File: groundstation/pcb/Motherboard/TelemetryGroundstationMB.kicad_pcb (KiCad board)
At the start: 4 copper layers, 95 x 95 mm, 146 parts, among them J1 USB-C, J2 USB-C, J3 RFPC-SMA28-F, J4 RFPC-SMA28-F, M1 M4 Mounting Hole, M2 M4 Mounting Hole, M3 M4 Mounting Hole, M4 M4 Mounting Hole, Q1 NPN, U1 CP2102N, U2 CP2102N, U3 RC1780HP-RC232, U4 RC1701HP-RC232, U5 AVR128DB64x-xPT, U6 W25Q80DVSSIG

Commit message: add motherboard pcb
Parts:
- removed C15: 1 uf, Capacitor_SMD:C_0805_2012Metric_Pad1.18x1.45mm_HandSolder
- removed D17: yellow, LED_SMD:LED_0805_2012Metric_Pad1.15x1.40mm_HandSolder
- removed D18: D, Diode_SMD:D_SOD-123
- removed D19, D20, D21, D22, D23, D24: red, LED_SMD:LED_0805_2012Metric_Pad1.15x1.40mm_HandSolder
- removed D25, D26: orange, LED_SMD:LED_0805_2012Metric_Pad1.15x1.40mm_HandSolder
- removed JL1: Stackable Socket 1x8, Footprints:JL1
- removed JL2: Stackable Socket 1x8, Footprints:JL2
- removed JL3: Stackable Socket 1x8, Footprints:JL3
- removed JL4: Stackable Socket 1x8, Footprints:JL4
- removed JR1: Stackable Socket 1x8, Footprints:JR1
- removed JR2: Stackable Socket 1x8, Footprints:JR2
- removed JR3: Stackable Socket 1x8, Footprints:JR3
- removed JR4: Stackable Socket 1x8, Footprints:JR4
- removed LS1: Buzzer CMT-0525-75-SMT-TR, Footprints:Buzzer XDCR_CMT-0525-75-SMT-TR
- removed Q1: NPN, Package_TO_SOT_SMD:SOT-23
- removed R40, R41, R42, R49, R50: 5k6, Resistor_SMD:R_0805_2012Metric_Pad1.20x1.40mm_HandSolder
- removed R43, R44: 1k, Resistor_SMD:R_0805_2012Metric_Pad1.20x1.40mm_HandSolder
- removed R45, R46: 270R, Resistor_SMD:R_0805_2012Metric_Pad1.20x1.40mm_HandSolder
- removed the REF** at (-9.00, 25.5)
- removed the REF** at (-23.5, 25.5)
- removed the REF** at (-12.0, 25.5)
- removed TP12, TP13, TP14, TP15, TP16, TP17, TP18, TP19, TP36, TP37, TP38, TP39, TP4, TP41, TP5, TP60, TP70, TP8, TP80, TP9: TestPoint, Footprints:Test Point
- removed ZP1, ZP2, ZS1, ZS2: ~, Resistor_SMD:R_0805_2012Metric_Pad1.20x1.40mm_HandSolder
- added ?: , , F.Cu at (35.2, 61.5)
- added ?: , , F.Cu at (35.2, 66.4)
- added C13: 100uF Elko, Capacitor_THT:CP_Radial_D6.3mm_P2.50mm, F.Cu at (57.0, 26.0)
- added C14: 100uF Elko, Capacitor_THT:CP_Radial_D6.3mm_P2.50mm, F.Cu at (83.0, 26.0)
- added D29: orange, LED_SMD:LED_0805_2012Metric_Pad1.15x1.40mm_HandSolder, F.Cu at (67.5, 66.0)
- added D30: orange, LED_SMD:LED_0805_2012Metric_Pad1.15x1.40mm_HandSolder, F.Cu at (65.0, 66.0)
- added D31: orange, LED_SMD:LED_0805_2012Metric_Pad1.15x1.40mm_HandSolder, F.Cu at (62.5, 66.0)
- added D32: orange, LED_SMD:LED_0805_2012Metric_Pad1.15x1.40mm_HandSolder, F.Cu at (60.0, 66.0)
- added D33: orange, LED_SMD:LED_0805_2012Metric_Pad1.15x1.40mm_HandSolder, F.Cu at (57.5, 66.0)
- added D34: orange, LED_SMD:LED_0805_2012Metric_Pad1.15x1.40mm_HandSolder, F.Cu at (55.0, 66.0)
- added J10: Conn_01x01, Footprints:Banana_CT3151-0, F.Cu at (23.5, 44.2)
- added J11: Conn_01x01, Footprints:Banana_CT3151-0, F.Cu at (7.25, 44.2)
- added J5: ICD15S13E4GV00LF, Footprints:AMPHENOL_ICD15S13E4GV00LF[1], F.Cu at (34.0, 0.00)
- added J6: ICD15S13E4GV00LF, Footprints:AMPHENOL_ICD15S13E4GV00LF[1], F.Cu at (0.00, 0.00)
- added J7: ICD15S13E4GV00LF, Footprints:AMPHENOL_ICD15S13E4GV00LF[1], F.Cu at (68.0, 0.00)
- added J8: LD09S33E4GV00LF, Footprints:AMPHENOL_LD09S33E4GV00LF, F.Cu at (-6.00, 30.0)
- added J9: Conn_01x04_Socket, Connector_PinSocket_2.54mm:PinSocket_1x04_P2.54mm_Vertical, F.Cu at (20.6, 20.8)
- added JP3: SolderJumper_2_Open, Footprints:Solder Jumper, F.Cu at (96.8, 19.5)
- added R22: 5k1, Resistor_SMD:R_0805_2012Metric, F.Cu at (108.2, 24.4)
- added R51: 560 Ohm, Resistor_SMD:R_0805_2012Metric_Pad1.20x1.40mm_HandSolder, F.Cu at (67.5, 61.0)
- added R52: 560 Ohm, Resistor_SMD:R_0805_2012Metric_Pad1.20x1.40mm_HandSolder, F.Cu at (65.0, 61.0)
- added R53: 560 Ohm, Resistor_SMD:R_0805_2012Metric_Pad1.20x1.40mm_HandSolder, F.Cu at (62.5, 61.0)
- added R54: 560 Ohm, Resistor_SMD:R_0805_2012Metric_Pad1.20x1.40mm_HandSolder, F.Cu at (60.0, 61.0)
- added R55: 560 Ohm, Resistor_SMD:R_0805_2012Metric_Pad1.20x1.40mm_HandSolder, F.Cu at (57.5, 61.0)
- added R56: 560 Ohm, Resistor_SMD:R_0805_2012Metric_Pad1.20x1.40mm_HandSolder, F.Cu at (55.0, 61.0)
- added REF**: Test Point Hole, Footprints:Test Point Hole, F.Cu at (92.7, 27.4)
- added REF**: Test Point Hole, Footprints:Test Point Hole, F.Cu at (92.7, 45.4)
- added REF**: Test Point Hole, Footprints:Test Point Hole, F.Cu at (92.7, 59.9)
- added REF**: Test Point Hole, Footprints:Test Point Hole, F.Cu at (92.7, 48.4)
- added REF**: Test Point Hole, Footprints:Test Point Hole, F.Cu at (92.7, 30.4)
- added SW1: SW_Push, Connector_PinSocket_2.54mm:PinSocket_1x02_P2.54mm_Vertical, F.Cu at (31.0, 31.0)
- added SW2: SW_Push, Connector_PinSocket_2.54mm:PinSocket_1x02_P2.54mm_Vertical, F.Cu at (27.0, 31.0)
- added SW3: SW_Push, Connector_PinSocket_2.54mm:PinSocket_1x02_P2.54mm_Vertical, F.Cu at (23.0, 31.0)
- added SW4: SW_Push, Connector_PinSocket_2.54mm:PinSocket_1x02_P2.54mm_Vertical, F.Cu at (19.0, 31.0)
- added SW5: SW_Push, Connector_PinSocket_2.54mm:PinSocket_1x02_P2.54mm_Vertical, F.Cu at (15.0, 31.0)
- added SW6: SW_Push, Connector_PinSocket_2.54mm:PinSocket_1x02_P2.54mm_Vertical, F.Cu at (11.0, 31.0)
- added SW7: SW_Push, Connector_PinSocket_2.54mm:PinSocket_1x02_P2.54mm_Vertical, F.Cu at (7.00, 33.5)
- added SW8: SW_DIP_x01, Connector_PinSocket_2.54mm:PinSocket_1x02_P2.54mm_Vertical, F.Cu at (3.00, 33.5)
- added TP6: TestPoint, Footprints:Test Point, F.Cu at (96.8, 27.4)
- added TP7: TestPoint, Footprints:Test Point, F.Cu at (96.8, 30.4)
- C5: value 1 nF -> 0.1 uF
- C6: value 1 uf -> 4.7 uF
- C7: value 1 nF -> 10uF Tantal; footprint Capacitor_SMD:C_0805_2012Metric_Pad1.18x1.45mm_HandSolder -> Footprints:CAPMP3216X180N
- C8: value 1 uf -> 10uF Tantal; footprint Capacitor_SMD:C_0805_2012Metric_Pad1.18x1.45mm_HandSolder -> Footprints:CAPMP3216X180N
- D14: value green -> SP0503BAHT; footprint LED_SMD:LED_0805_2012Metric_Pad1.15x1.40mm_HandSolder -> Package_TO_SOT_SMD:SOT-143
- D15: value yellow -> green
- D16: value green -> orange
- J3: value RFPC-SMA28-F -> ICD15S13E4GV00LF; footprint Footprints:RFPC-SMA28-F -> Footprints:AMPHENOL_ICD15S13E4GV00LF[1]; moved to F.Cu
- J4: value RFPC-SMA28-F -> USB-C; footprint Footprints:RFPC-SMA28-F -> Footprints:GCT_USB4216-03-A_REVA; moved to F.Cu
- R23: value 2k7 -> 22k; footprint Resistor_SMD:R_0805_2012Metric_Pad1.20x1.40mm_HandSolder -> Resistor_SMD:R_0805_2012Metric
- R24: value 560R -> 47k; footprint Resistor_SMD:R_0805_2012Metric_Pad1.20x1.40mm_HandSolder -> Resistor_SMD:R_0805_2012Metric
- R25: value 560R -> 560 Ohm; footprint Resistor_SMD:R_0805_2012Metric_Pad1.20x1.40mm_HandSolder -> Resistor_SMD:R_0805_2012Metric
- R26: value 2k7 -> 560 Ohm; footprint Resistor_SMD:R_0805_2012Metric_Pad1.20x1.40mm_HandSolder -> Resistor_SMD:R_0805_2012Metric
- R27: value 560R -> 5k1; footprint Resistor_SMD:R_0805_2012Metric_Pad1.20x1.40mm_HandSolder -> Resistor_SMD:R_0805_2012Metric
- R28: value 560R -> 5k6
- R29: value 180 R -> 5k6
- R32, R33, R35, R36: value 1k -> 5k6
- R37: value 5k6 -> 560 Ohm
- R47, R48: value 270R -> 560 Ohm
- U3: value RC1780HP-RC232 -> CP2102N; footprint Footprints:Radiocrafts RC1780HP-RC232 -> Footprints:QFN20_CP2102N_SIL
- U4: value RC1701HP-RC232 -> MIC29300-5WU-TR; footprint Footprints:Radiocrafts RC1780HP-RC232 -> Footprints:MIC29300
- U6: value W25Q80DVSSIG -> MIC29300-3.3WU-TR; footprint Package_SO:SOIC-8_5.3x5.3mm_P1.27mm -> Footprints:MIC29300
- moved R48 179.6 mm to (70.0, 61.0), turned to 90 degrees
- moved D28 163.1 mm to (70.0, 66.0), turned to 90 degrees
- moved M2 152.0 mm to (113.0, 9.00)
- moved R26 147.7 mm to (104.8, 31.4), turned to 180 degrees
- moved R29 144.5 mm to (28.0, 26.5)
- moved D9 141.6 mm to (110.2, 65.9), turned to 0 degrees
- moved R23 137.8 mm to (103.8, 16.5), turned to 180 degrees
- moved R17 137.2 mm to (104.8, 65.9), turned to 180 degrees
- moved J2 134.8 mm to (113.9, 56.9), turned to 90 degrees
- moved R13 133.7 mm to (108.2, 60.4), turned to -90 degrees
- moved R18 132.0 mm to (100.2, 64.4), turned to 90 degrees
- moved R30 131.6 mm to (21.6, 16.8)
- moved D10 131.0 mm to (95.2, 66.4), turned to 180 degrees
- moved R31 128.6 mm to (17.1, 16.8), turned to 180 degrees
- moved R19 127.8 mm to (95.9, 63.5), turned to 0 degrees
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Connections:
- C5 pad 1: Net-(U3-RESET) -> +3V3
- C7 pad 1: Net-(U4-RESET) -> +3V3
- C8 pad 1: +3V3 -> +5V
- D14 pad 2: Net-(D14-A) -> VBUS3
- D15 pad 1: GND -> Net-(D15-K)
- D15 pad 2: Net-(D15-A) -> +3V3
- D16 pad 1: GND -> Net-(D16-K)
- D16 pad 2: Net-(D16-A) -> +3V3
- J3 pad 1: Net-(J3-Pad1) -> TX0
- R23 pad 1: Net-(U3-RESET) -> VBUS3
- R23 pad 2: RST1 -> Net-(U3-VBUS)
- R24 pad 1: Net-(D14-A) -> Net-(U3-VBUS)
- R24 pad 2: Net-(U3-D1) -> GND
- R25 pad 1: Net-(D15-A) -> Net-(D15-K)
- R25 pad 2: Net-(U3-D2) -> Net-(U3-~{TXT}/GPIO.2)
- R26 pad 1: Net-(U4-RESET) -> Net-(D16-K)
- R26 pad 2: RST2 -> Net-(U3-~{RXT}/GPIO.3)
- R27 pad 1: Net-(D16-A) -> Net-(J4-CC2)
- R27 pad 2: Net-(U4-D1) -> GND
- R28 pad 1: Net-(D17-A) -> Button1
- R28 pad 2: Net-(U4-D2) -> GND
- R29 pad 1: Net-(Q1-B) -> Button2
- R29 pad 2: BUZZ -> GND
- R30 pad 1: SCL1 -> SCL0
- R31 pad 1: SDA1 -> SDA0
- R32 pad 1: Net-(D19-K) -> Button3
- R32 pad 2: TX0 -> GND
- R33 pad 1: RX0 -> Button4
- R33 pad 2: Net-(D20-K) -> GND
- R34 pad 1: TX0 -> Button5
- R34 pad 2: +3V3 -> GND
- R35 pad 1: Net-(D21-K) -> Button6
- R35 pad 2: TX1 -> GND
- R36 pad 1: RX1 -> MasterButton
- R36 pad 2: Net-(D22-K) -> GND
- R37 pad 1: TX1 -> +3V3
- R37 pad 2: +3V3 -> Net-(R37-Pad2)
- R38 pad 1: RST1 -> Input1
- R38 pad 2: +3V3 -> GND
- R39 pad 1: RST2 -> Input2
- R39 pad 2: +3V3 -> GND
- R48 pad 2: Net-(U5-PD6) -> Net-(U5-PD1)
- TP1 pad 1: RX4 -> RX5
- TP2 pad 1: TX4 -> TX5
- U1 pad 17: TX4 -> TX5
- U1 pad 18: RX4 -> RX5
- U3 pad 1: GND -> unconnected-(U3-RS485/GPIO.1-Pad1)
- U3 pad 10: GND -> unconnected-(U3-NC-Pad10)
- U3 pad 12: Net-(U3-RESET) -> GND
- U3 pad 13: +3V3 -> unconnected-(U3-~{WAKEUP}-Pad13)
- U3 pad 14: GND -> unconnected-(U3-SUSPEND-Pad14)
- U3 pad 15: unconnected-(U3-Pad15) -> Net-(JP3-A)
- U3 pad 17: unconnected-(U3-Pad17) -> TX2
- U3 pad 18: unconnected-(U3-Pad18) -> RX2
- U3 pad 19: unconnected-(U3-DD-Pad19) -> Net-(U3-~{RXT}/GPIO.3)
- U3 pad 2: CTS1 -> unconnected-(U3-CLK/GPIO.0-Pad2)
- U3 pad 20: unconnected-(U3-DC-Pad20) -> Net-(U3-~{TXT}/GPIO.2)
- U3 pad 21: unconnected-(U3-Pad21) -> GND
- U3 pad 3: RTS1 -> GND
- U3 pad 4: CFG1 -> D+3
- U3 pad 5: RX0 -> D-3
- U3 pad 6: TX0 -> +3V3
- U3 pad 7: GND -> +3V3
- U3 pad 8: GND -> Net-(U3-VBUS)
- U3 pad 9: Net-(U3-RF) -> unconnected-(U3-~{RST}-Pad9)
- U4 pad 2: CTS2 -> +BATT
- U4 pad 3: RTS2 -> +5V
- U4 pad 4: CFG2 -> GND
- U5 pad 1: RST1 -> D01
- U5 pad 10: unconnected-(U5-PB2-Pad10) -> D33
- U5 pad 11: unconnected-(U5-PB3-Pad11) -> D32
- U5 pad 12: RST2 -> D31
- U5 pad 13: RTS2 -> D34
- U5 pad 14: CTS2 -> unconnected-(U5-PB6-Pad14)
- U5 pad 15: CFG2 -> unconnected-(U5-PB7-Pad15)
- U5 pad 18: SDA1 -> D13
- U5 pad 19: SCL1 -> D12
- U5 pad 22: D4 -> D11
- U5 pad 23: D5 -> D14
- U5 pad 24: unconnected-(U5-PC6-Pad24) -> SDA0
- U5 pad 25: unconnected-(U5-PC7-Pad25) -> SCL0
- U5 pad 27: unconnected-(U5-PD1-Pad27) -> Net-(U5-PD1)
- U5 pad 29: unconnected-(U5-PD3-Pad29) -> Net-(U5-PD3)
- U5 pad 31: unconnected-(U5-PD5-Pad31) -> Net-(U5-PD5)
- U5 pad 33: unconnected-(U5-VREFA/PD7-Pad33) -> Net-(U5-VREFA/PD7)
- U5 pad 36: MOSI0 -> TX4
- U5 pad 37: MISO0 -> RX4
- U5 pad 38: SCK0 -> D23
- U5 pad 39: CS0 -> D22
- U5 pad 4: CTS1 -> D04
- U5 pad 40: TX4 -> D21
- U5 pad 41: RX4 -> D24
- U5 pad 42: LED B -> Input2
- U5 pad 43: LED G -> Input1
- U5 pad 44: LED R -> TX2
- U5 pad 45: LED 1 -> RX2
- U5 pad 46: LED 2 -> Button6
- U5 pad 47: LED 3 -> Button5
- U5 pad 48: D26 -> Button4
- U5 pad 49: D27 -> Button3
- U5 pad 5: CFG1 -> unconnected-(U5-PA7-Pad5)
- U5 pad 50: D28 -> Button2
- U5 pad 52: SLP -> TX5
- U5 pad 53: ARM1 -> RX5
- U5 pad 54: unconnected-(U5-PG2-Pad54) -> Button1
- U5 pad 55: unconnected-(U5-PG3-Pad55) -> LED B
- U5 pad 58: unconnected-(U5-PG4-Pad58) -> LED G
- U5 pad 59: unconnected-(U5-PG5-Pad59) -> LED R
- U5 pad 60: unconnected-(U5-PG6-Pad60) -> LED 3
- U5 pad 61: unconnected-(U5-PG7-Pad61) -> LED 2
- U5 pad 62: unconnected-(U5-XTALHF1/PA0-Pad62) -> LED 1
- U5 pad 63: unconnected-(U5-XTALHF2/PA1-Pad63) -> D03
- U5 pad 64: unconnected-(U5-PA2-Pad64) -> D02
- U5 pad 8: RTS1 -> TX3
- U5 pad 9: BUZZ -> RX3
- U6 pad 1: CS0 -> GND
- U6 pad 2: MISO0 -> +BATT
- U6 pad 3: unconnected-(U6-~{WP}/IO_{2}-Pad3) -> +3V3
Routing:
- net RX2: track 0.00 -> 120.7 mm, vias 0 -> 2
- net TX2: track 0.00 -> 119.7 mm, vias 0 -> 2
- net RX5: track 0.00 -> 100.8 mm, vias 0 -> 2
- net TX5: track 0.00 -> 99.3 mm, vias 0 -> 2
- net UPDI: track 7.61 -> 102.0 mm, vias 0 -> 2
- net D03: track 0.00 -> 76.2 mm
- net D02: track 0.00 -> 72.6 mm
- net TX0: track 0.00 -> 70.5 mm
- net Net-(U5-PD0): track 0.00 -> 67.8 mm, vias 0 -> 2
- net D01: track 0.00 -> 67.5 mm
- net Net-(U5-PD1): track 0.00 -> 67.0 mm, vias 0 -> 2
- net Net-(U5-PD2): track 0.00 -> 66.1 mm, vias 0 -> 2
- net Net-(U5-PD3): track 0.00 -> 65.3 mm, vias 0 -> 2
- net RX0: track 0.00 -> 64.6 mm
- net Net-(U5-PD4): track 0.00 -> 64.5 mm, vias 0 -> 2
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- removed copper zone on In2.Cu, net +3V3
- removed copper zone on In1.Cu, net GND
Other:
- board size 95 x 95 mm -> 133 x 79.8 mm
- copper layers 4 -> 2
- board text removed: "01"
- board text removed: "02"
- board text removed: "03"
- board text removed: "04"
- board text removed: "05"
- board text removed: "06"
- board text removed: "07"
- board text removed: "08"
- board text removed: "09"
- board text removed: "0x??"
- board text removed: "1"
- board text removed: "10"
- board text removed: "11"
- board text removed: "12"
- board text removed: "13"
- board text removed: "14"
- board text removed: "15"
- board text removed: "16"
- board text removed: "17"
- board text removed: "18"
- board text removed: "19"
- board text removed: "2"
- board text removed: "20"
- board text removed: "21"
- board text removed: "22"
- board text removed: "23"
- board text removed: "24"
- board text removed: "25"
- board text removed: "26"
- board text removed: "27"
- board text removed: "28"
- board text removed: "29"
- board text removed: "3"
- board text removed: "30"
- board text removed: "31"
- board text removed: "32"
- board text removed: "3V3"
- board text removed: "4"
- board text removed: "5V"
- board text removed: "ARM1"
- board text removed: "ARM2"
- board text removed: "BAT"
- board text removed: "D26"
- board text removed: "D27"
- board text removed: "D28"
- board text removed: "D4"
- board text removed: "D5"
- board text removed: "GND"
- board text removed: "LP"
- board text removed: "PWR"
- board text removed: "RX"
- board text removed: "SCL"
- board text removed: "SDA"
- board text removed: "SLP"
- board text removed: "SPROG ASCENT III MODUL vx.y.z"
- board text removed: "Serial Number:"
- board text removed: "TX"

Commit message: add power traces to motherboard pcb
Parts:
- moved C10 126.3 mm to (146.8, 90.8)
- moved C13 122.6 mm to (155.5, 99.0)
- moved C14 122.6 mm to (181.5, 98.9)
- moved C12 122.4 mm to (143.8, 87.0)
- moved ? 122.0 mm to (133.7, 133.5)
- moved ? 122.0 mm to (133.7, 138.4)
- moved C1 122.0 mm to (200.0, 110.5)
- moved C11 122.0 mm to (128.0, 78.5)
- moved C2 122.0 mm to (200.0, 108.5)
- moved C3 122.0 mm to (200.0, 128.5)
- moved C4 122.0 mm to (200.0, 126.5)
- moved C5 122.0 mm to (200.0, 90.5)
- moved C6 122.0 mm to (200.0, 92.5)
- moved C7 122.0 mm to (140.0, 106.0)
- moved C8 122.0 mm to (165.5, 106.0)
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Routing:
- net +3V3: track 62.3 -> 470.8 mm, vias 8 -> 14
- net +5V: track 17.7 -> 221.0 mm
- net +BATT: track 20.9 -> 200.9 mm, vias 0 -> 2
- net GND: track 9.67 -> 22.7 mm, vias 12 -> 15
- net D+3: vias 1 -> 2
- net D+1: vias 3 -> 2
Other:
- board text added: "Licensed under CERN-OHL-S v2 or any later version: ohwr.org/cern_ohl_s_v2.txt The source files can be found at: github.com/ Spaceflight-Rocketry-Giessen-e-V/ Telemetry"
- board text added: "SPROG ASCENT III TELEMETRY v1.0.0 Motherboard"
- board text added: "Serial Number:"

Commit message: move some vias on Motherboard
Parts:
- moved D27 6.50 mm to (164.5, 138.0)
- moved D28 6.50 mm to (162.0, 138.0)
- moved D29 6.50 mm to (159.5, 138.0)
- moved D30 6.50 mm to (157.0, 138.0)
- moved D31 6.50 mm to (154.5, 138.0)
- moved D32 6.50 mm to (152.0, 138.0)
- moved D33 6.50 mm to (149.5, 138.0)
- moved D34 6.50 mm to (147.0, 138.0)
- moved R47 6.50 mm to (164.5, 133.0)
- moved R48 6.50 mm to (162.0, 133.0)
- moved R51 6.50 mm to (159.5, 133.0)
- moved R52 6.50 mm to (157.0, 133.0)
- moved R53 6.50 mm to (154.5, 133.0)
- moved R54 6.50 mm to (152.0, 133.0)
- moved R55 6.50 mm to (149.5, 133.0)
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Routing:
- net RX2: track 120.7 -> 131.5 mm
- net Net-(U5-VREFA/PD7): track 61.1 -> 58.4 mm
- net Net-(U5-PD5): track 63.7 -> 60.9 mm
- net Net-(U5-PD4): track 64.5 -> 61.8 mm
- net Net-(U5-PD2): track 66.1 -> 63.4 mm
- net Net-(U5-PD1): track 67.0 -> 64.2 mm
- net Net-(U5-PD3): track 65.3 -> 62.6 mm
- net Net-(U5-PD6): track 62.8 -> 60.2 mm
- net RX5: track 100.8 -> 103.3 mm
- net TX5: track 99.3 -> 101.4 mm
- net +3V3: track 470.8 -> 472.4 mm
- net Net-(U5-PD0): track 67.8 -> 66.2 mm
- net TX2: track 119.7 -> 120.4 mm
- net GND: vias 15 -> 16

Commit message: add power supply via USB to Motherboard
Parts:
- removed C14: 100uF Elko, Capacitor_THT:CP_Radial_D6.3mm_P2.50mm
- removed C8: 10uF Tantal, Footprints:CAPMP3216X180N
- removed U4: MIC29300-5WU-TR, Footprints:MIC29300
- added J12: USB-C, Footprints:GCT_USB4216-03-A_REVA, F.Cu at (170.9, 136.2)
- added R40: 5k1, Resistor_SMD:R_0805_2012Metric_Pad1.20x1.40mm_HandSolder, F.Cu at (168.6, 130.0)
- added R41: 5k1, Resistor_SMD:R_0805_2012Metric_Pad1.20x1.40mm_HandSolder, F.Cu at (173.6, 130.0)
- moved D11 37.4 mm to (176.0, 109.0), turned to -90 degrees
- moved R20 34.7 mm to (176.0, 114.0), turned to 90 degrees
- moved C7 30.6 mm to (167.8, 118.8), turned to 0 degrees
- moved D13 25.3 mm to (177.8, 119.5)
- moved C13 20.8 mm to (155.2, 119.8), turned to 180 degrees
- moved D12 17.4 mm to (179.5, 109.0), turned to -90 degrees
- moved R21 15.9 mm to (179.5, 114.0), turned to 90 degrees
- moved U6 14.7 mm to (163.0, 105.8), turned to 90 degrees
- moved C10 9.61 mm to (138.3, 90.2)
- moved ? 3.04 mm to (130.7, 133.0)
- moved ? 3.04 mm to (130.7, 137.9)
- moved C1 3.04 mm to (197.0, 110.0)
- moved C11 3.04 mm to (125.0, 78.0)
- moved C2 3.04 mm to (197.0, 108.0)
- moved C3 3.04 mm to (197.0, 128.0)
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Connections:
- C13 pad 1: +BATT -> +5V
- J11 pad 1: +BATT -> +5V
- U6 pad 2: +BATT -> +5V
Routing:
- net +BATT: track 200.9 -> 0.00 mm, vias 2 -> 0
- net +5V: track 221.0 -> 359.3 mm, vias 0 -> 3
- net +3V3: track 472.4 -> 440.2 mm, vias 14 -> 12
- net GND: track 22.7 -> 32.4 mm
- net RX2: track 131.5 -> 122.0 mm
- net Net-(J12-CC2): track 0.00 -> 2.82 mm
- net Net-(J12-CC1): track 0.00 -> 2.82 mm
- net Net-(D11-A): track 1.95 -> 3.00 mm
- net RX5: track 103.3 -> 103.8 mm
- net Net-(D12-A): track 2.47 -> 2.97 mm
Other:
- board text added: "D34-D27"
- board text added: "R56-R47"
- board text added: "SPROG e.V. Motherboard Telemetry v1.0.0"
- board text removed: "SPROG ASCENT III TELEMETRY v1.0.0 Motherboard"

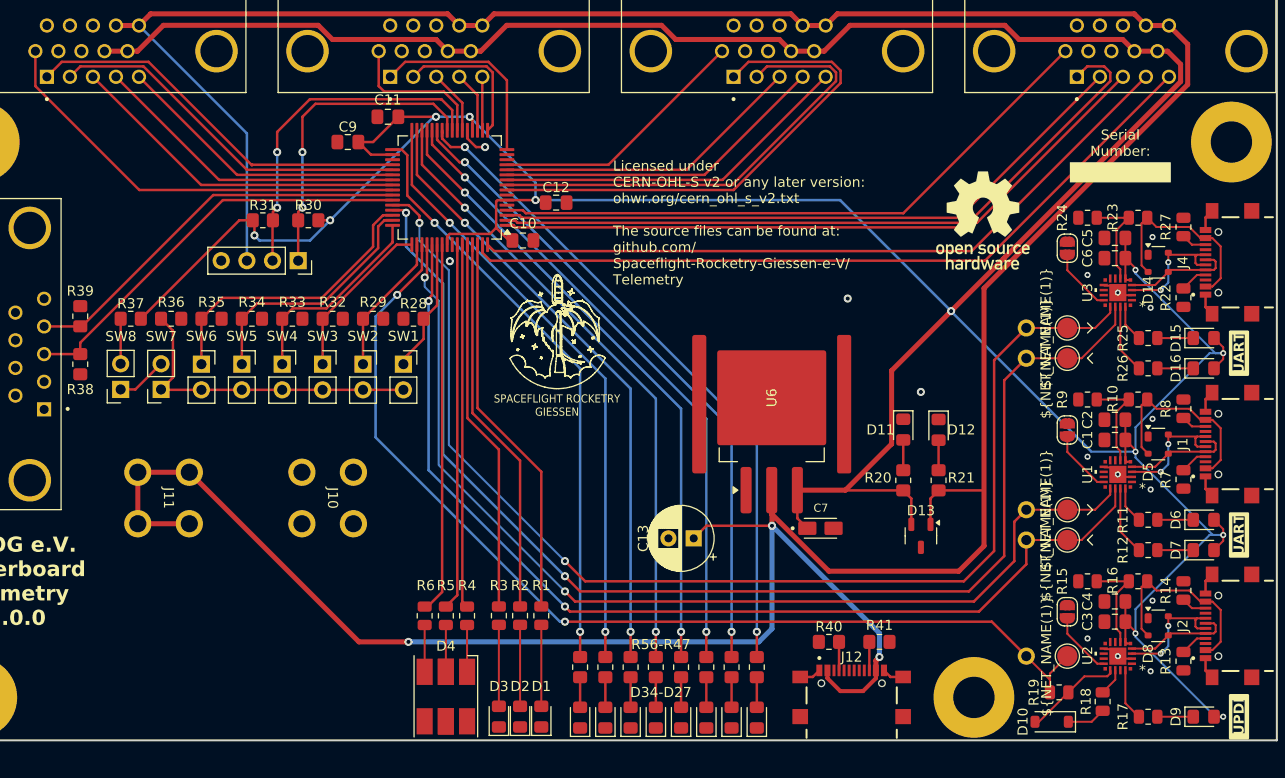
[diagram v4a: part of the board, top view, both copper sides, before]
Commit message: update Motherboard (only cosmetical)
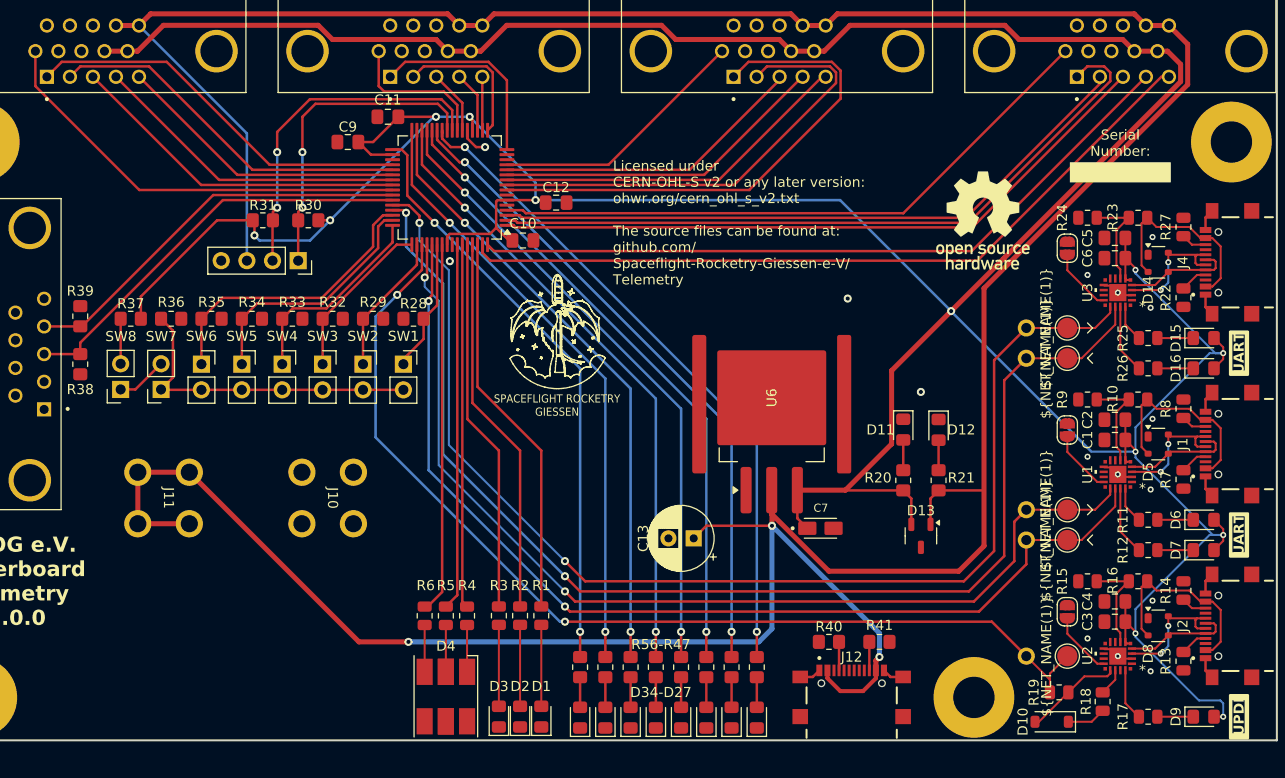
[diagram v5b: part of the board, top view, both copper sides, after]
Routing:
- net +3V3: track 440.2 -> 442.2 mm
- net TX3: track 50.2 -> 51.1 mm
